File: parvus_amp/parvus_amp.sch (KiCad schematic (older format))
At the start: 45 parts, among them J1 ctrl, J2 input, J3 output, J4 power, U1 TDA7293

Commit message: Added Mouser ID for AL capacitors.
Signed-off-by: Nenad Radulovic <nenad.b.radulovic@gmail.com>
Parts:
- C1, C2: Manufacturer Multicomp: MCGPR35V106M5X11 -> (none); Manufacturer1 (none) -> Multicomp: MCGPR35V106M5X11; Manufacturer2 (none) -> Nichicon: UVZ1V100MDD1TD; Supplier2 (none) -> Mouser: 647-UVZ1V100MDD1TD
- C11, C14: Manufacturer Rybicon: 50YXJ2200M16X35.5 -> (none); Manufacturer1 (none) -> Rybicon: 50YXJ2200M16X35.5; Manufacturer2 (none) -> Nichicon: UPW1V222MHD; Supplier2 (none) -> Mouser: 647-UPW1V222MHD
- C4: Manufacturer Rybicon: 63YXJ47M6.3X11 -> (none); Manufacturer1 (none) -> Rybicon: 63YXJ47M6.3X11; Manufacturer2 (none) -> Nichicon: UPW1H470MED; Supplier2 (none) -> Mouser: 647-UPW1H470MED
- C6: Manufacturer Rybicon: 50YXJ3R3M5X11 -> (none); Manufacturer1 (none) -> Rybicon: 50YXJ3R3M5X11; Manufacturer2 (none) -> Nichicon: UPW2A3R3MDD; Supplier2 (none) -> Mouser: 647-UPW2A3R3MDD
- C7: footprint Capacitor_THT:CP_Radial_D6.3mm_P2.50mm -> Capacitor_THT:CP_Radial_D8.0mm_P3.50mm; Manufacturer Rybicon:10YXJ470M6.3X11 -> (none); Manufacturer1 (none) -> Rybicon:10YXJ470M6.3X11; Manufacturer2 (none) -> Nichicon: UPW0J471MPD; Supplier2 (none) -> Mouser: 647-UPW0J471MPD
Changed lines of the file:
@@
 F 0 "C7" V 3563 3200 50  0000 C CNN
 F 1 "470u" V 3654 3200 50  0000 C CNN
-F 2 "Capacitor_THT:CP_Radial_D6.3mm_P2.50mm" H 3438 3050 50  0001 C CNN
+F 2 "Capacitor_THT:CP_Radial_D8.0mm_P3.50mm" H 3438 3050 50  0001 C CNN
 F 3 "http://www.farnell.com/datasheets/2321616.pdf" H 3400 3200 50  0001 C CNN
 F 4 "10V" V 3745 3200 50  0000 C CNN "Voltage"
-F 5 "Rybicon:10YXJ470M6.3X11 " V 3400 3200 50  0001 C CNN "Manufacturer"
-F 6 "Farnell: 2346252" V 3400 3200 50  0001 C CNN "Supplier1"
+F 5 "Farnell: 2346252" V 3400 3200 50  0001 C CNN "Supplier1"
+F 6 "Rybicon:10YXJ470M6.3X11 " H 0   0   50  0001 C CNN "Manufacturer1"
+F 7 "Nichicon: UPW0J471MPD" H 0   0   50  0001 C CNN "Manufacturer2"
+F 8 "Mouser:  647-UPW0J471MPD" H 0   0   50  0001 C CNN "Supplier2"
 	1    3400 3200
 	0    1    1    0
@@
 F 3 "http://www.farnell.com/datasheets/1723232.pdf" H 7100 1850 50  0001 C CNN
 F 4 "35V" H 6982 1759 50  0000 R CNN "Voltage"
-F 5 "Multicomp: MCGPR35V106M5X11" H 7100 1850 50  0001 C CNN "Manufacturer"
+F 5 "" H 7100 1850 50  0001 C CNN "Manufacturer"
 F 6 "Farnell: 9451242" H 7100 1850 50  0001 C CNN "Supplier1"
+F 7 "Multicomp: MCGPR35V106M5X11" H 0   0   50  0001 C CNN "Manufacturer1"
+F 8 "Nichicon: UVZ1V100MDD1TD" H 0   0   50  0001 C CNN "Manufacturer2"
+F 9 "Mouser:  647-UVZ1V100MDD1TD" H 0   0   50  0001 C CNN "Supplier2"
 	1    7100 1850
 	-1   0    0    -1
@@
 F 3 "http://www.farnell.com/datasheets/2321616.pdf" H 3400 2700 50  0001 C CNN
 F 4 "50V" V 3237 2700 50  0000 C CNN "Voltage"
-F 5 "Rybicon: 50YXJ3R3M5X11" H 3400 2700 50  0001 C CNN "Manufacturer"
-F 6 "Farnell: 2346267" H 3400 2700 50  0001 C CNN "Supplier1"
+F 5 "Farnell: 2346267" H 3400 2700 50  0001 C CNN "Supplier1"
+F 6 "Rybicon: 50YXJ3R3M5X11" H 0   0   50  0001 C CNN "Manufacturer1"
+F 7 "Nichicon: UPW2A3R3MDD" H 0   0   50  0001 C CNN "Manufacturer2"
+F 8 "Mouser:  647-UPW2A3R3MDD " H 0   0   50  0001 C CNN "Supplier2"
 	1    3400 2700
 	0    1    1    0
@@
 F 3 "http://www.farnell.com/datasheets/2321616.pdf" H 6500 2650 50  0001 C CNN
 F 4 "63V" H 6382 2559 50  0000 R CNN "Voltage"
-F 5 "Rybicon: 63YXJ47M6.3X11" H 6500 2650 50  0001 C CNN "Manufacturer"
-F 6 "Farnell: 2346274" H 6500 2650 50  0001 C CNN "Supplier1"
+F 5 "Farnell: 2346274" H 6500 2650 50  0001 C CNN "Supplier1"
+F 6 "Rybicon: 63YXJ47M6.3X11" H 6500 2650 50  0001 C CNN "Manufacturer1"
+F 7 "Mouser:  647-UPW1H470MED" H 6500 2650 50  0001 C CNN "Supplier2"
+F 8 "Nichicon: UPW1H470MED" H 6500 2650 50  0001 C CNN "Manufacturer2"
 	1    6500 2650
 	-1   0    0    -1
@@
 F 3 "http://www.farnell.com/datasheets/2321616.pdf" H 2200 6250 50  0001 C CNN
 F 4 "50V" H 2082 6159 50  0000 R CNN "Voltage"
-F 5 "Rybicon: 50YXJ2200M16X35.5" V 2200 6250 50  0001 C CNN "Manufacturer"
-F 6 "Farnell: 2346272" V 2200 6250 50  0001 C CNN "Supplier1"
+F 5 "Farnell: 2346272" V 2200 6250 50  0001 C CNN "Supplier1"
+F 6 "Rybicon: 50YXJ2200M16X35.5" H 0   0   50  0001 C CNN "Manufacturer1"
+F 7 "Nichicon: UPW1V222MHD" H 0   0   50  0001 C CNN "Manufacturer2"
+F 8 "Mouser:  647-UPW1V222MHD" H 0   0   50  0001 C CNN "Supplier2"
 	1    2200 6250
 	-1   0    0    -1
@@
 F 3 "http://www.farnell.com/datasheets/1723232.pdf" H 7600 1850 50  0001 C CNN
 F 4 "35V" H 7482 1759 50  0000 R CNN "Voltage"
-F 5 "Multicomp: MCGPR35V106M5X11" H 7600 1850 50  0001 C CNN "Manufacturer"
+F 5 "" H 7600 1850 50  0001 C CNN "Manufacturer"
 F 6 "Farnell: 9451242" H 7600 1850 50  0001 C CNN "Supplier1"
+F 7 "Multicomp: MCGPR35V106M5X11" H 0   0   50  0001 C CNN "Manufacturer1"
+F 8 "Nichicon: UVZ1V100MDD1TD" H 0   0   50  0001 C CNN "Manufacturer2"
+F 9 "Mouser:  647-UVZ1V100MDD1TD" H 0   0   50  0001 C CNN "Supplier2"
 	1    7600 1850
 	-1   0    0    -1
@@
 F 3 "http://www.farnell.com/datasheets/2321616.pdf" H 2200 6750 50  0001 C CNN
 F 4 "50V" H 2082 6659 50  0000 R CNN "Voltage"
-F 5 "Rybicon: 50YXJ2200M16X35.5" V 2200 6750 50  0001 C CNN "Manufacturer"
-F 6 "Farnell: 2346272" V 2200 6750 50  0001 C CNN "Supplier1"
+F 5 "Farnell: 2346272" V 2200 6750 50  0001 C CNN "Supplier1"
+F 6 "Rybicon: 50YXJ2200M16X35.5" H 0   0   50  0001 C CNN "Manufacturer1"
+F 7 "Nichicon: UPW1V222MHD" H 0   0   50  0001 C CNN "Manufacturer2"
+F 8 "Mouser:  647-UPW1V222MHD" H 0   0   50  0001 C CNN "Supplier2"
 	1    2200 6750
 	-1   0    0    -1

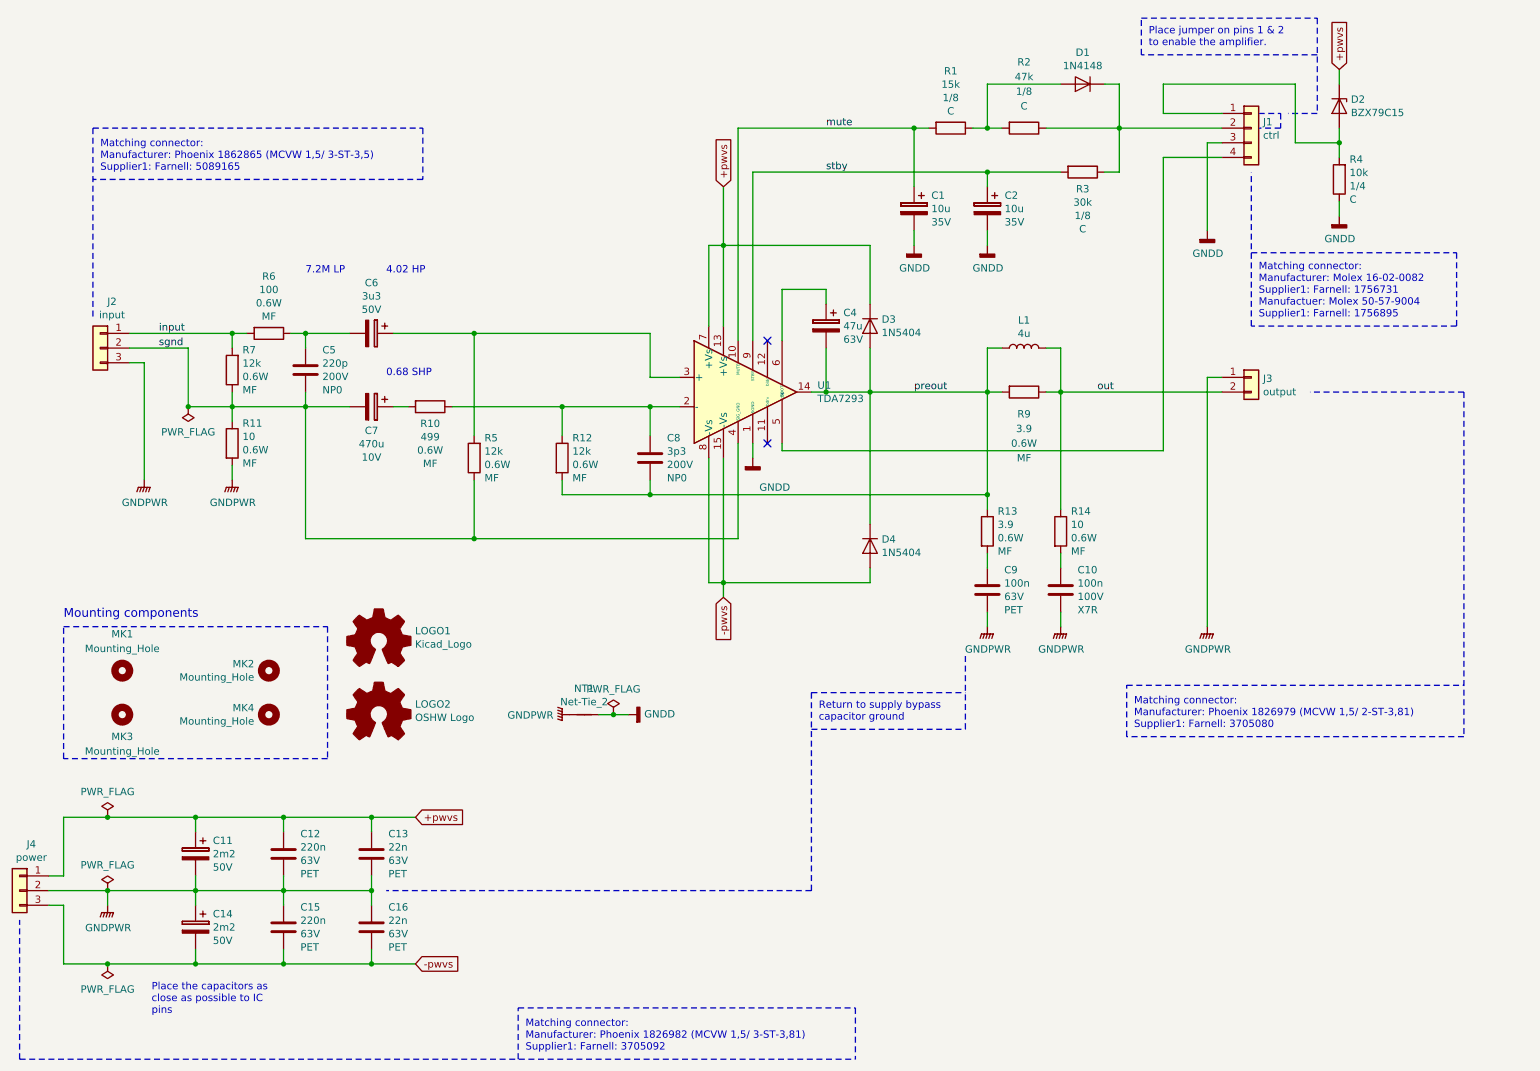
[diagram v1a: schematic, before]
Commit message: Adjusted NFB capacitor footprint and rest of Mouser IDs.
Signed-off-by: Nenad Radulovic <nenad.b.radulovic@gmail.com>
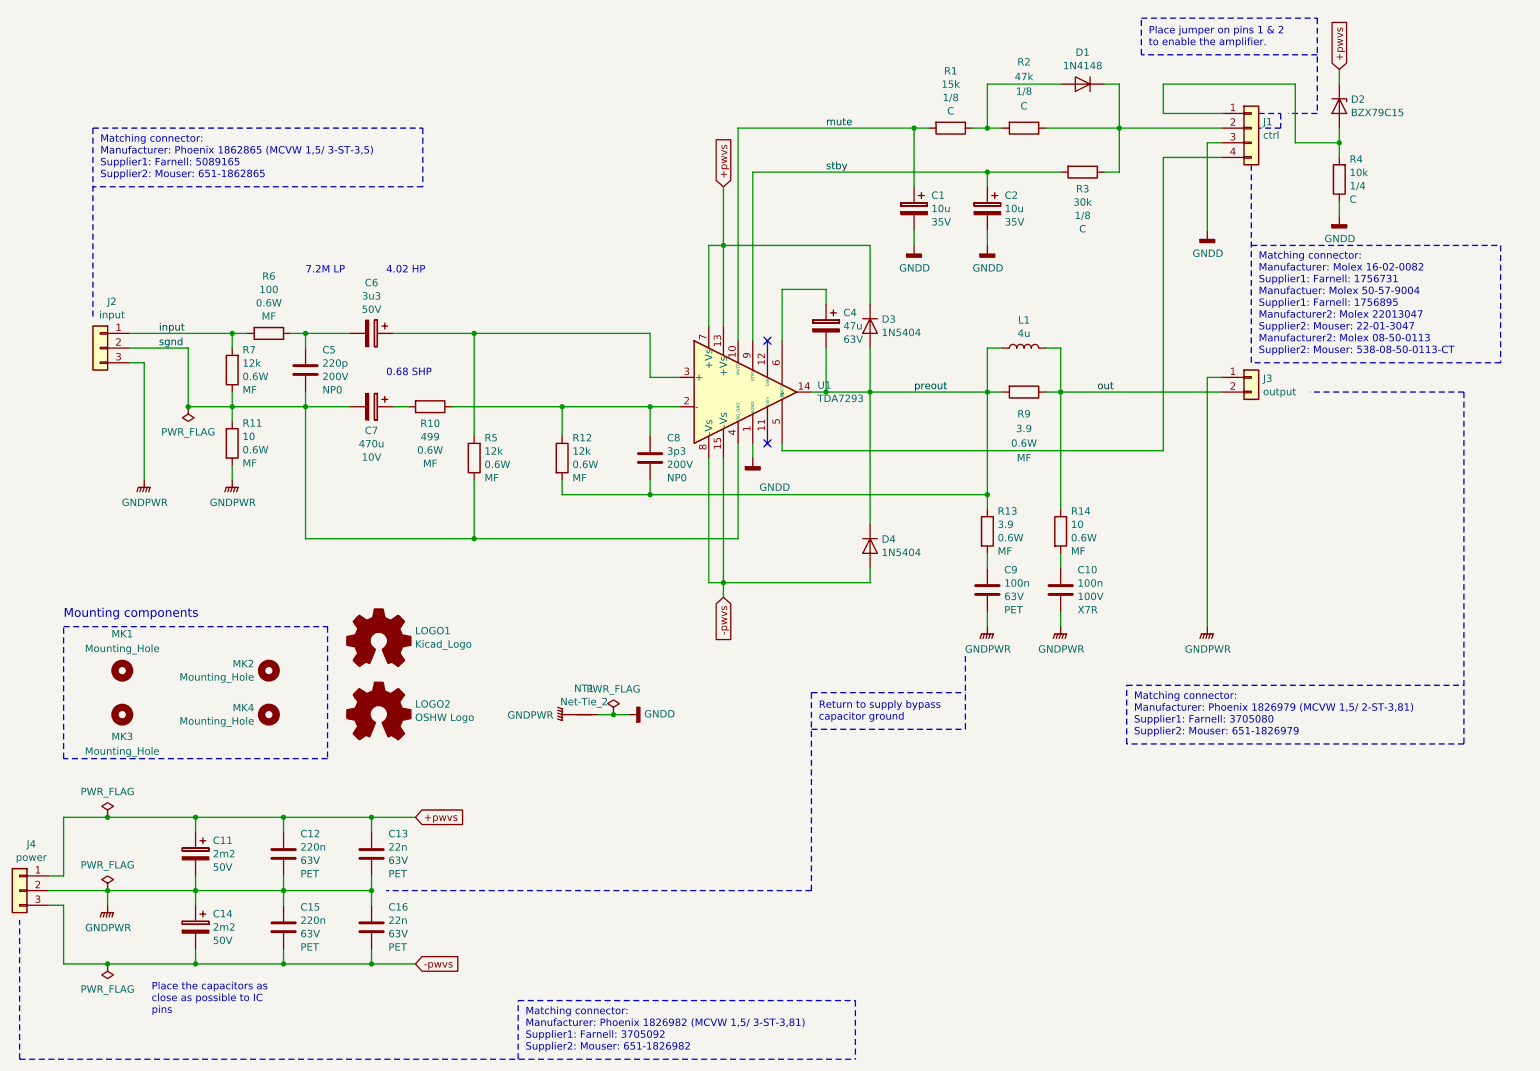
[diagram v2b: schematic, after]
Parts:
- J1: Manufacturer1 (none) -> Molex: 171856-0004; Supplier1 (none) -> Mouser: 538-171856-0004
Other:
- note added: "Matching connector:\nManufacturer: Molex 16-02-0082\nSupplier1: Farnell: 1756731\nManufactuer: Molex 50-57-9004\nSupplier1: Farnell: 1756895\nManufacturer2: Molex 22013047\nSupplier2: Mouser: 22-01-3047\nManufacturer2: Molex 08-50-0113\nSupplier2: Mouser: 538-08-50-0113-CT"
- note added: "Matching connector:\nManufacturer: Phoenix 1826979 (MCVW 1,5/ 2-ST-3,81)\nSupplier1: Farnell: 3705080\nSupplier2: Mouser: 651-1826979"
- note added: "Matching connector:\nManufacturer: Phoenix 1826982 (MCVW 1,5/ 3-ST-3,81)\nSupplier1: Farnell: 3705092\nSupplier2: Mouser: 651-1826982"
- note added: "Matching connector:\nManufacturer: Phoenix 1862865 (MCVW 1,5/ 3-ST-3,5)\nSupplier1: Farnell: 5089165\nSupplier2: Mouser: 651-1862865"
- note removed: "Matching connector:\nManufacturer: Molex 16-02-0082\nSupplier1: Farnell: 1756731\nManufactuer: Molex 50-57-9004\nSupplier1: Farnell: 1756895"
- note removed: "Matching connector:\nManufacturer: Phoenix 1826979 (MCVW 1,5/ 2-ST-3,81)\nSupplier1: Farnell: 3705080"
- note removed: "Matching connector:\nManufacturer: Phoenix 1826982 (MCVW 1,5/ 3-ST-3,81)\nSupplier1: Farnell: 3705092"
- note removed: "Matching connector:\nManufacturer: Phoenix 1862865 (MCVW 1,5/ 3-ST-3,5)\nSupplier1: Farnell: 5089165"
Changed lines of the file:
@@
 Sheet 1 1
 Title "Parvus Power Amplifier"
-Date "2018-08-02"
+Date "2019-03-25"
 Rev "1.0"
 Comp "Real-Time Consulting"
@@
 F 4 "1/8" V 8547 1600 50  0000 C CNN "Power"
 F 5 "C" V 8638 1600 50  0000 C CNN "Type"
-F 6 "" V 8250 1600 50  0001 C CNN "Manufacturer"
-F 7 "Farnell: 9343008" V 8250 1600 50  0001 C CNN "Supplier1"
-F 8 "Multicomp: MF12 30K" H 0   0   50  0001 C CNN "Manufacturer1"
+F 6 "Farnell: 9343008" V 8250 1600 50  0001 C CNN "Supplier1"
+F 7 "Multicomp: MF12 30K" H 0   0   50  0001 C CNN "Manufacturer1"
+F 8 "Mouser: 603-CFR-25JR-52-30K" H 0   0   50  0001 C CNN "Supplier2"
 F 9 "Yageo: CFR-25JR-52-30K" H 0   0   50  0001 C CNN "Manufacturer2"
-F 10 "Mouser: 603-CFR-25JR-52-30K" H 0   0   50  0001 C CNN "Supplier2"
 	1    8250 1600
 	0    1    1    0
@@
 F 4 "1/8" V 7600 1300 50  0000 C CNN "Power"
 F 5 "C" V 7700 1300 50  0000 C CNN "Type"
-F 6 "" V 7850 1300 50  0001 C CNN "Manufacturer"
-F 7 "Farnell: 9343261" V 7850 1300 50  0001 C CNN "Supplier1"
-F 8 "Multicomp: MF12 47K" H 0   0   50  0001 C CNN "Manufacturer1"
+F 6 "Farnell: 9343261" V 7850 1300 50  0001 C CNN "Supplier1"
+F 7 "Multicomp: MF12 47K" H 0   0   50  0001 C CNN "Manufacturer1"
+F 8 "Mouser: 603-CFR-25JR-5247K" H 0   0   50  0001 C CNN "Supplier2"
 F 9 "Yageo: CFR-25JR-52-47K" H 0   0   50  0001 C CNN "Manufacturer2"
-F 10 "Mouser: 603-CFR-25JR-5247K" H 0   0   50  0001 C CNN "Supplier2"
 	1    7850 1300
 	0    1    1    0
@@
 F 2 "Connector_PinHeader_2.54mm:PinHeader_1x04_P2.54mm_Vertical" H 9400 1300 50  0001 C CNN
 F 3 "http://www.farnell.com/datasheets/2697192.pdf" H 9400 1300 50  0001 C CNN
-F 4 "~" H 9400 1300 50  0001 C CNN "Manufacturer"
-F 5 "~" H 9400 1300 50  0001 C CNN "Supplier1"
+F 4 "Molex:  171856-0004" H 9400 1300 50  0001 C CNN "Manufacturer1"
+F 5 "Mouser: 538-171856-0004" H 9400 1300 50  0001 C CNN "Supplier1"
 	1    9400 1300
 	1    0    0    -1
@@
 F 4 "1/4" H 9930 1695 50  0000 R CNN "Power"
 F 5 "C" H 9930 1786 50  0000 R CNN "Type"
-F 6 "" V 10000 1650 50  0001 C CNN "Manufacturer"
-F 7 "Farnell: 9341110" V 10000 1650 50  0001 C CNN "Supplier1"
-F 8 "Multicomp: MF25 10K" H 0   0   50  0001 C CNN "Manufacturer1"
+F 6 "Farnell: 9341110" V 10000 1650 50  0001 C CNN "Supplier1"
+F 7 "Multicomp: MF25 10K" H 0   0   50  0001 C CNN "Manufacturer1"
+F 8 "Mouser: 603-CFR-25JR-5210K" H 0   0   50  0001 C CNN "Supplier2"
 F 9 "Yageo: CFR-25JR-52-10K" H 0   0   50  0001 C CNN "Manufacturer2"
-F 10 "Mouser: 603-CFR-25JR-5210K" H 0   0   50  0001 C CNN "Supplier2"
 	1    10000 1650
 	-1   0    0    1
@@
 F 4 "1/8" V 7143 1300 50  0000 C CNN "Power"
 F 5 "C" V 7234 1300 50  0000 C CNN "Type"
-F 6 "" V 7350 1300 50  0001 C CNN "Manufacturer"
-F 7 "Farnell: 9342630" V 7350 1300 50  0001 C CNN "Supplier1"
-F 8 "Multicomp: MF12 15K" H 0   0   50  0001 C CNN "Manufacturer1"
+F 6 "Farnell: 9342630" V 7350 1300 50  0001 C CNN "Supplier1"
+F 7 "Multicomp: MF12 15K" H 0   0   50  0001 C CNN "Manufacturer1"
+F 8 "Mouser: 603-CFR-25JR-5215K" H 0   0   50  0001 C CNN "Supplier2"
 F 9 "Yageo: CFR-25JR-52-15K" H 0   0   50  0001 C CNN "Manufacturer2"
-F 10 "Mouser: 603-CFR-25JR-5215K" H 0   0   50  0001 C CNN "Supplier2"
 	1    7350 1300
 	0    1    1    0
@@
 Text Notes 2950 2300 0    50   ~ 0
 7.2M LP
-Text Notes 9450 2600 0    50   ~ 0
-Matching connector:\nManufacturer: Molex 16-02-0082\nSupplier1: Farnell: 1756731\nManufactuer: Molex 50-57-9004\nSupplier1: Farnell: 1756895
-Text Notes 1550 1600 0    50   ~ 0
-Matching connector:\nManufacturer: Phoenix 1862865 (MCVW 1,5/ 3-ST-3,5)\nSupplier1: Farnell: 5089165
-Text Notes 8600 5400 0    50   ~ 0
-Matching connector:\nManufacturer: Phoenix 1826979 (MCVW 1,5/ 2-ST-3,81)\nSupplier1: Farnell: 3705080
+Text Notes 9450 2850 0    50   ~ 0
+Matching connector:\nManufacturer: Molex 16-02-0082\nSupplier1: Farnell: 1756731\nManufactuer: Molex 50-57-9004\nSupplier1: Farnell: 1756895\nManufacturer2: Molex 22013047\nSupplier2: Mouser: 22-01-3047\nManufacturer2: Molex 08-50-0113\nSupplier2: Mouser: 538-08-50-0113-CT
+Text Notes 1550 1650 0    50   ~ 0
+Matching connector:\nManufacturer: Phoenix 1862865 (MCVW 1,5/ 3-ST-3,5)\nSupplier1: Farnell: 5089165\nSupplier2: Mouser: 651-1862865
+Text Notes 8600 5450 0    50   ~ 0
+Matching connector:\nManufacturer: Phoenix 1826979 (MCVW 1,5/ 2-ST-3,81)\nSupplier1: Farnell: 3705080\nSupplier2: Mouser: 651-1826979
 Text Notes 4450 7600 0    50   ~ 0
-Matching connector:\nManufacturer: Phoenix 1826982 (MCVW 1,5/ 3-ST-3,81)\nSupplier1: Farnell: 3705092
+Matching connector:\nManufacturer: Phoenix 1826982 (MCVW 1,5/ 3-ST-3,81)\nSupplier1: Farnell: 3705092\nSupplier2: Mouser: 651-1826982
 Text Label 6500 1300 0    50   ~ 0
 mute
@@
 	8550 5100 10850 5100
 Wire Notes Line
-	10850 5450 8550 5450
-Wire Notes Line
-	8550 5450 8550 5100
+	10850 5500 8550 5500
+Wire Notes Line
+	8550 5500 8550 5100
 Wire Notes Line
 	10850 3100 9800 3100
 Wire Notes Line
-	10850 3100 10850 5450
-Wire Notes Line
-	9400 2150 10800 2150
-Wire Notes Line
-	10800 2150 10800 2650
-Wire Notes Line
-	10800 2650 9400 2650
-Wire Notes Line
-	9400 2650 9400 1600
-Wire Notes Line
-	4400 7300 6700 7300
-Wire Notes Line
-	6700 7300 6700 7650
-Wire Notes Line
-	4400 7650 4400 7300
+	10850 3100 10850 5500
+Wire Notes Line
+	9400 2100 11100 2100
+Wire Notes Line
+	11100 2100 11100 2900
+Wire Notes Line
+	11100 2900 9400 2900
+Wire Notes Line
+	9400 2900 9400 1550
+Wire Notes Line
+	4400 7250 6700 7250
+Wire Notes Line
+	6700 7250 6700 7650
+Wire Notes Line
+	4400 7650 4400 7250
 Wire Notes Line
 	1000 7650 1000 6700
@@
 	1500 1300 3750 1300
 Wire Notes Line
-	3750 1300 3750 1650
-Wire Notes Line
-	3750 1650 1500 1650
+	3750 1300 3750 1700
+Wire Notes Line
+	3750 1700 1500 1700
 Wire Notes Line
 	1500 1300 1500 2600

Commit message: Minor tweaks to schematic and PCB.
Signed-off-by: Nenad Radulovic <nenad.b.radulovic@gmail.com>
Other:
- note added: "Place the capacitors as\nclose as possible to IC\npower supply pins."
- note removed: "Place the capacitors as\nclose as possible to IC\npins"
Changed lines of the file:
@@
 AR Path="/5C37C649" Ref="U1"  Part="1"
 AR Path="/5C37BC7C/5C37C649" Ref="U?"  Part="1"
-F 0 "U1" H 6441 3146 50  0000 L CNN
-F 1 "TDA7293" H 6441 3055 50  0000 L CNN
+F 0 "U1" H 5250 3800 50  0000 L CNN
+F 1 "TDA7293" H 5250 3700 50  0000 L CNN
 F 2 "Package_TO_SOT_THT:TO-220-15_P2.54x2.54mm_StaggerOdd_Lead4.58mm_Vertical" H 6000 3100 50  0001 C CIN
 F 3 "http://www.farnell.com/datasheets/1761334.pdf" H 6000 3100 50  0001 C CNN
@@
 Return to supply bypass \ncapacitor ground
 Text Notes 1900 7350 0    50   ~ 0
-Place the capacitors as\nclose as possible to IC\npins
+Place the capacitors as\nclose as possible to IC\npower supply pins.
 $Comp
 L Device:CP C7
@@
 U 1 1 5C55F742
 P 4850 5300
-F 0 "NT1" H 4850 5478 50  0000 C CNN
-F 1 "Net-Tie_2" H 4850 5387 50  0000 C CNN
+F 0 "NT1" H 4850 5250 50  0000 C CNN
+F 1 "Net-Tie_2" H 4850 5150 50  0000 C CNN
 F 2 "NetTie:NetTie-2_SMD_Pad2.0mm" H 4850 5300 50  0001 C CNN
 F 3 "~" H 4850 5300 50  0001 C CNN
